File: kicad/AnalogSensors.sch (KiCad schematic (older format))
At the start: 7 parts, among them P201 CONN_01X01, P202 CONN_01X01

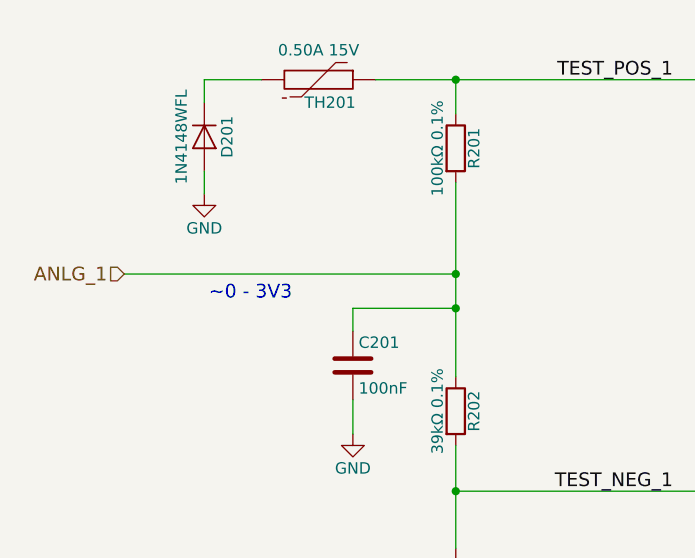
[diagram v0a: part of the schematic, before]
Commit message: added the missing pullup resistors 2L_2
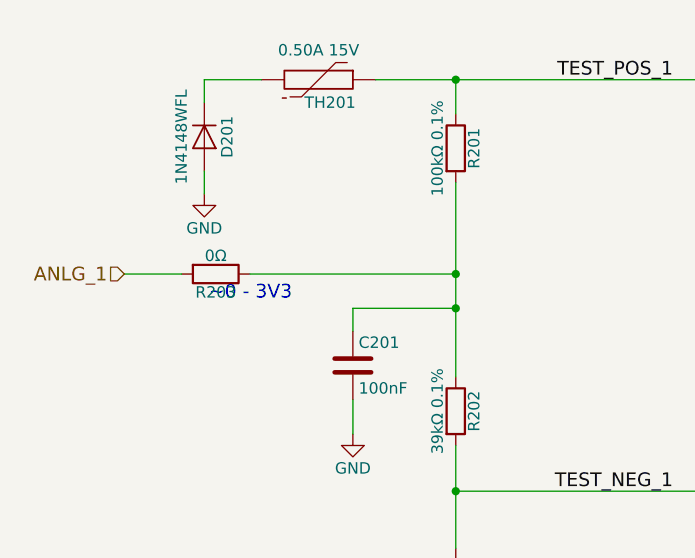
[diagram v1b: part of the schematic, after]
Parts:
- added R203: 0Ω, Resistors_SMD:R_0805, symbol R
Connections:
- net ANLG_1: now also R203.2; no longer C201.1, R201.2, R202.1
- new net: C201.1, R201.2, R202.1, R203.1
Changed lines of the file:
@@
 $EndComp
 $Comp
-L GND #PWR06
+L GND #PWR07
 U 1 1 593EDD91
 P 3500 3450
-F 0 "#PWR06" H 3500 3200 50  0001 C CNN
+F 0 "#PWR07" H 3500 3200 50  0001 C CNN
 F 1 "GND" H 3500 3300 50  0000 C CNN
 F 2 "" H 3500 3450 50  0000 C CNN
@@
 $EndComp
 $Comp
-L GND #PWR07
+L GND #PWR08
 U 1 1 593EDDA0
 P 2400 1900
-F 0 "#PWR07" H 2400 1650 50  0001 C CNN
+F 0 "#PWR08" H 2400 1650 50  0001 C CNN
 F 1 "GND" H 2400 1750 50  0000 C CNN
 F 2 "" H 2400 1900 50  0000 C CNN
@@
 $EndComp
 $Comp
-L GND #PWR08
+L GND #PWR09
 U 1 1 593EDDCB
 P 3050 2950
-F 0 "#PWR08" H 3050 2700 50  0001 C CNN
+F 0 "#PWR09" H 3050 2700 50  0001 C CNN
 F 1 "GND" H 3050 2800 50  0000 C CNN
 F 2 "" H 3050 2950 50  0000 C CNN
@@
 Connection ~ 3500 2400
 Wire Wire Line
-	2050 2250 3500 2250
-Connection ~ 3500 2250
-Wire Wire Line
 	3500 3200 4600 3200
 Connection ~ 3500 3200
@@
 	1    0    0    -1
 $EndComp
+$Comp
+L R R203
+U 1 1 595D4DB1
+P 2450 2250
+F 0 "R203" V 2530 2250 50  0000 C CNN
+F 1 "0Ω" V 2370 2250 50  0000 C CNN
+F 2 "Resistors_SMD:R_0805" V 2380 2250 50  0001 C CNN
+F 3 "" H 2450 2250 50  0000 C CNN
+F 4 "Value" H 2450 2250 60  0001 C CNN "Link"
+	1    2450 2250
+	0    1    1    0
+$EndComp
+Wire Wire Line
+	2050 2250 2300 2250
+Wire Wire Line
+	2600 2250 3500 2250
+Connection ~ 3500 2250
 $EndSCHEMATC

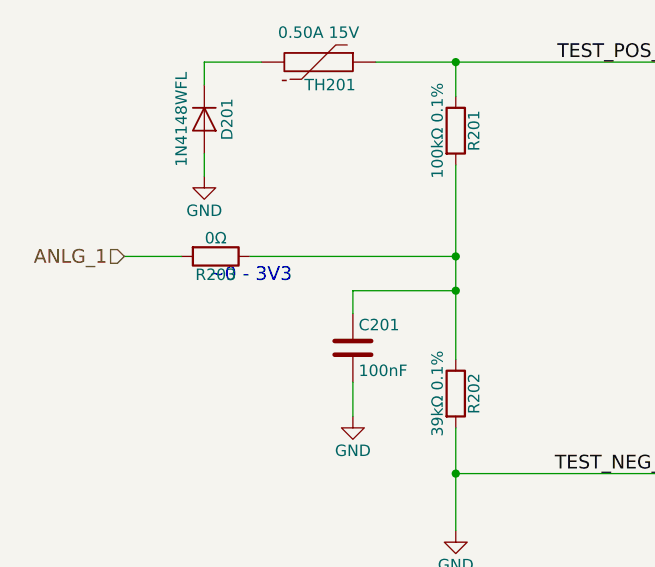
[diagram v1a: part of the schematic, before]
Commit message: Corrected the usage of the CE_Header to be front-side only
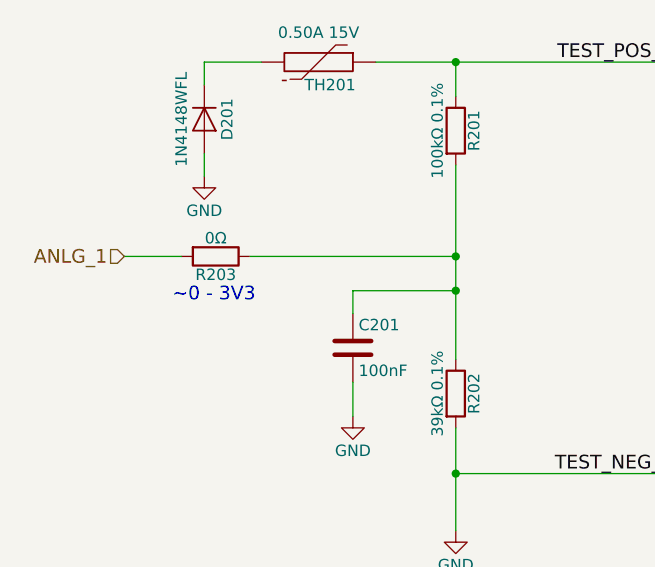
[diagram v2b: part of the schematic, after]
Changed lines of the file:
@@
 Text Notes 5000 1400 0    60   ~ 0
 +12V
-Text Notes 2420 2370 0    60   ~ 0
+Text Notes 2260 2455 0    60   ~ 0
 ~~0 - 3V3
 $Comp

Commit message: Testing the idea of a zenner on the V Input. Added test code for the voltage test
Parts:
- added D?: 3V3, symbol ZENER
- D201: Link Value -> https://www.digikey.de/products/de?keywords=1N4148WFL-G3-08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
- P201: value CONN_01X01 -> Positive
- P202: value CONN_01X01 -> Negative
- TH201: Link Value -> https://www.digikey.de/product-detail/de/bourns-inc/MF-MSMF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
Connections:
- wire segments 13 -> 15
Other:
- note added: "\nThe 12v input is to be converted to 0-3v3 for a Teency Ananlog input.\n\nThe diode (D201) and a thermistor (TH201) as a form of protection should \nthe input be reversed.\n\nIn addition, to protect the Teency Analog input. (The are 5V tolerant but \nwill cap the reading for anything above 3V3). To that end, a 3V3 Zenner \ncould help. Anything higher than the 12V is not expected, but possibly \n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"
- moved on the sheet: C201, R201, R202
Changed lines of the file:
@@
 L R R201
 U 1 1 593EDD83
-P 3500 1700
-F 0 "R201" V 3580 1700 50  0000 C CNN
-F 1 "100kΩ 0.1%" V 3420 1700 50  0000 C CNN
-F 2 "Resistors_SMD:R_1206" V 3430 1700 50  0001 C CNN
-F 3 "" H 3500 1700 50  0000 C CNN
-F 4 "SPR-1206 100K" H 3500 1700 60  0001 C CNN "MPN"
-F 5 "Value" H 3500 1700 60  0001 C CNN "Link"
-	1    3500 1700
+P 3500 1800
+F 0 "R201" V 3580 1800 50  0000 C CNN
+F 1 "100kΩ 0.1%" V 3420 1800 50  0000 C CNN
+F 2 "Resistors_SMD:R_1206" V 3430 1800 50  0001 C CNN
+F 3 "" H 3500 1800 50  0000 C CNN
+F 4 "SPR-1206 100K" H 3500 1800 60  0001 C CNN "MPN"
+F 5 "Value" H 3500 1800 60  0001 C CNN "Link"
+	1    3500 1800
 	1    0    0    -1
 $EndComp
@@
 L R R202
 U 1 1 593EDD8A
-P 3500 2850
-F 0 "R202" V 3580 2850 50  0000 C CNN
-F 1 "39kΩ 0.1%" V 3420 2850 50  0000 C CNN
-F 2 "Resistors_SMD:R_1206" V 3430 2850 50  0001 C CNN
-F 3 "" H 3500 2850 50  0000 C CNN
-F 4 "SPR-1206 39,0K" H 3500 2850 60  0001 C CNN "MPN"
-F 5 "Value" H 3500 2850 60  0001 C CNN "Link"
-	1    3500 2850
+P 3500 2700
+F 0 "R202" V 3580 2700 50  0000 C CNN
+F 1 "39kΩ 0.1%" V 3420 2700 50  0000 C CNN
+F 2 "Resistors_SMD:R_1206" V 3430 2700 50  0001 C CNN
+F 3 "" H 3500 2700 50  0000 C CNN
+F 4 "SPR-1206 39,0K" H 3500 2700 60  0001 C CNN "MPN"
+F 5 "Value" H 3500 2700 60  0001 C CNN "Link"
+	1    3500 2700
 	1    0    0    -1
 $EndComp
@@
 F 1 "1N4148WFL" H 2400 1550 50  0000 C CNN
 F 2 "FieldDevice_Footprints:D_SOD-123" H 2400 1650 50  0001 C CNN
-F 3 "" H 2400 1650 50  0000 C CNN
+F 3 "https://media.digikey.com/pdf/Data%20Sheets/Vishay%20Semiconductors/1N4148WFL-G.pdf" H 2400 1650 50  0001 C CNN
 F 4 "1N4148WFL-G3-08GICT-ND" H 2400 1650 60  0001 C CNN "MPN"
-F 5 "Value" H 2400 1650 60  0001 C CNN "Link"
+F 5 "https://www.digikey.de/products/de?keywords=1N4148WFL-G3-08GICT-ND" H 2400 1650 60  0001 C CNN "Link"
 	1    2400 1650
 	0    1    1    0
@@
 F 3 "http://www.bourns.com/docs/Product-Datasheets/mfmsmf.pdf" H 2900 1400 50  0001 C CNN
 F 4 "MF-MSMF050-2" H 2900 1400 60  0001 C CNN "MPN"
-F 5 "Value" H 2900 1400 60  0001 C CNN "Link"
+F 5 "https://www.digikey.de/product-detail/de/bourns-inc/MF-MSMF050-2/MF-MSMF050-2TR-ND/662816" H 2900 1400 60  0001 C CNN "Link"
 	1    2900 1400
 	0    1    1    0
@@
 L C C201
 U 1 1 593EDDC1
-P 3050 2650
-F 0 "C201" H 3075 2750 50  0000 L CNN
-F 1 "100nF" H 3075 2550 50  0000 L CNN
-F 2 "Capacitors_SMD:C_0805" H 3088 2500 30  0001 C CNN
-F 3 "" H 3050 2650 60  0000 C CNN
-	1    3050 2650
+P 3950 2500
+F 0 "C201" H 3975 2600 50  0000 L CNN
+F 1 "100nF" H 3975 2400 50  0000 L CNN
+F 2 "Capacitors_SMD:C_0805" H 3988 2350 30  0001 C CNN
+F 3 "" H 3950 2500 60  0000 C CNN
+	1    3950 2500
 	1    0    0    -1
 $EndComp
@@
 L GND #PWR09
 U 1 1 593EDDCB
-P 3050 2950
-F 0 "#PWR09" H 3050 2700 50  0001 C CNN
-F 1 "GND" H 3050 2800 50  0000 C CNN
-F 2 "" H 3050 2950 50  0000 C CNN
-F 3 "" H 3050 2950 50  0000 C CNN
-	1    3050 2950
+P 3950 2700
+F 0 "#PWR09" H 3950 2450 50  0001 C CNN
+F 1 "GND" H 3950 2550 50  0000 C CNN
+F 2 "" H 3950 2700 50  0000 C CNN
+F 3 "" H 3950 2700 50  0000 C CNN
+	1    3950 2700
 	1    0    0    -1
 $EndComp
@@
 	3150 1400 4600 1400
 Wire Wire Line
-	3500 1400 3500 1550
+	3500 1400 3500 1650
 Connection ~ 3500 1400
 Wire Wire Line
-	3500 1850 3500 2700
-Wire Wire Line
-	3500 3000 3500 3450
-Wire Wire Line
-	3050 2800 3050 2950
-Wire Wire Line
-	3050 2500 3050 2400
-Wire Wire Line
-	3050 2400 3500 2400
-Connection ~ 3500 2400
+	3500 1950 3500 2550
+Wire Wire Line
+	3500 2850 3500 3450
+Wire Wire Line
+	3950 2650 3950 2700
+Wire Wire Line
+	3950 2300 3950 2350
 Wire Wire Line
 	3500 3200 4600 3200
@@
 P 4800 1400
 F 0 "P201" H 4800 1500 50  0000 C CNN
-F 1 "CONN_01X01" V 4900 1400 50  0000 C CNN
+F 1 "Positive" H 4800 1300 50  0000 C CNN
 F 2 "Pin_Headers:Pin_Header_Straight_1x01_Pitch2.54mm" H 4800 1400 60  0001 C CNN
 F 3 "" H 4800 1400 60  0000 C CNN
@@
 P 4800 3200
 F 0 "P202" H 4800 3300 50  0000 C CNN
-F 1 "CONN_01X01" V 4900 3200 50  0000 C CNN
+F 1 "Negative" H 4800 3100 50  0000 C CNN
 F 2 "Pin_Headers:Pin_Header_Straight_1x01_Pitch2.54mm" H 4800 3200 60  0001 C CNN
 F 3 "" H 4800 3200 60  0000 C CNN
@@
 	2600 2250 3500 2250
 Connection ~ 3500 2250
+Wire Wire Line
+	3500 2300 3950 2300
+Connection ~ 3500 2300
+$Comp
+L GND #PWR?
+U 1 1 598F2A3D
+P 3050 3150
+F 0 "#PWR?" H 3050 2900 50  0001 C CNN
+F 1 "GND" H 3050 3000 50  0000 C CNN
+F 2 "" H 3050 3150 50  0000 C CNN
+F 3 "" H 3050 3150 50  0000 C CNN
+	1    3050 3150
+	1    0    0    -1
+$EndComp
+$Comp
+L ZENER D?
+U 1 1 598F27BC
+P 3050 2750
+F 0 "D?" H 3050 2850 50  0000 C CNN
+F 1 "3V3" H 3050 2650 50  0000 C CNN
+F 2 "" H 3050 2750 60  0000 C CNN
+F 3 "http://www.onsemi.com/pub/Collateral/BZX84C2V4LT1-D.PDF" H 3050 2750 60  0001 C CNN
+F 4 "BZX84C3V3LT1G" H 3050 2750 60  0001 C CNN "MPN"
+F 5 "https://www.digikey.de/product-detail/de/on-semiconductor/BZX84C3V3LT1G/BZX84C3V3LT1GOSTR-ND/918402" H 3050 2750 60  0001 C CNN "Link"
+	1    3050 2750
+	0    1    1    0
+$EndComp
+Wire Wire Line
+	3050 2550 3050 2250
+Connection ~ 3050 2250
+Wire Wire Line
+	3050 3150 3050 2950
+Text Notes 4750 2600 0    40   ~ 0
+\nThe 12v input is to be converted to 0-3v3 for a Teency Ananlog input.\n\nThe diode (D201) and a thermistor (TH201) as a form of protection should \nthe input be reversed.\n\nIn addition, to protect the Teency Analog input. (The are 5V tolerant but \nwill cap the reading for anything above 3V3). To that end, a 3V3 Zenner \ncould help. Anything higher than the 12V is not expected, but possibly \nupto 14V might be possible.\n\nTesting this circute, over 5V was seen when the input exceeded 18V
+Text Notes 3550 2150 0    60   ~ 0
+~~0 - 3V3
 $EndSCHEMATC

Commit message: Some changes to the test firmware and removed the Zenner
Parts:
- removed D?: 3V3, symbol ZENER
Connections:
- wire segments 15 -> 13
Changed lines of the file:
@@
 	3500 2300 3950 2300
 Connection ~ 3500 2300
-$Comp
-L GND #PWR?
-U 1 1 598F2A3D
-P 3050 3150
-F 0 "#PWR?" H 3050 2900 50  0001 C CNN
-F 1 "GND" H 3050 3000 50  0000 C CNN
-F 2 "" H 3050 3150 50  0000 C CNN
-F 3 "" H 3050 3150 50  0000 C CNN
-	1    3050 3150
-	1    0    0    -1
-$EndComp
-$Comp
-L ZENER D?
-U 1 1 598F27BC
-P 3050 2750
-F 0 "D?" H 3050 2850 50  0000 C CNN
-F 1 "3V3" H 3050 2650 50  0000 C CNN
-F 2 "" H 3050 2750 60  0000 C CNN
-F 3 "http://www.onsemi.com/pub/Collateral/BZX84C2V4LT1-D.PDF" H 3050 2750 60  0001 C CNN
-F 4 "BZX84C3V3LT1G" H 3050 2750 60  0001 C CNN "MPN"
-F 5 "https://www.digikey.de/product-detail/de/on-semiconductor/BZX84C3V3LT1G/BZX84C3V3LT1GOSTR-ND/918402" H 3050 2750 60  0001 C CNN "Link"
-	1    3050 2750
-	0    1    1    0
-$EndComp
-Wire Wire Line
-	3050 2550 3050 2250
-Connection ~ 3050 2250
-Wire Wire Line
-	3050 3150 3050 2950
 Text Notes 4750 2600 0    40   ~ 0
 \nThe 12v input is to be converted to 0-3v3 for a Teency Ananlog input.\n\nThe diode (D201) and a thermistor (TH201) as a form of protection should \nthe input be reversed.\n\nIn addition, to protect the Teency Analog input. (The are 5V tolerant but \nwill cap the reading for anything above 3V3). To that end, a 3V3 Zenner \ncould help. Anything higher than the 12V is not expected, but possibly \nupto 14V might be possible.\n\nTesting this circute, over 5V was seen when the input exceeded 18V
